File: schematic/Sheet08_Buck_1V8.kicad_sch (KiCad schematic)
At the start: 15 parts, among them U6 ISL70003ASEH

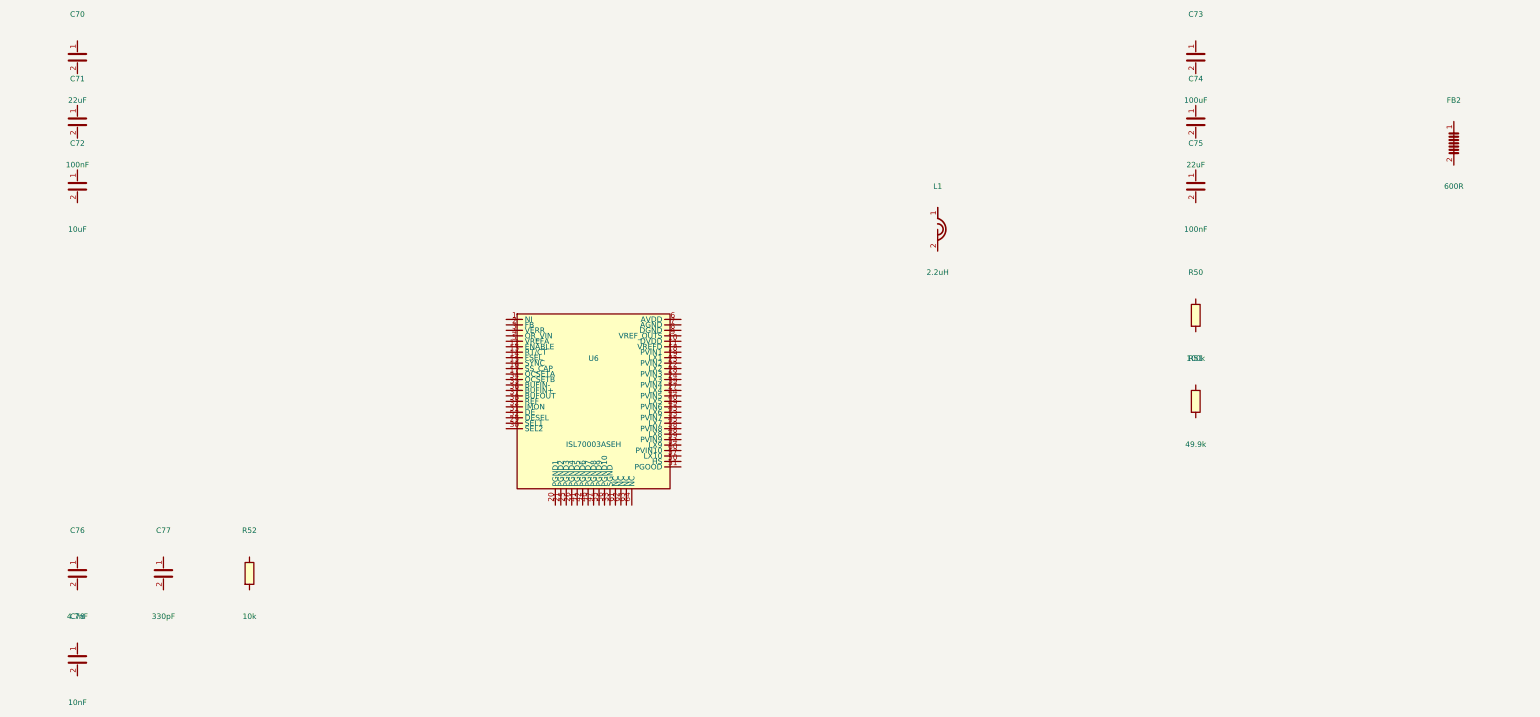
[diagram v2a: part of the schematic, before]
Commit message: feat: add 745 wire connections linking all IC pins to labels and power symbols
- Added stub wires from every component pin to net labels/global_labels
- Power pins connected to correct power symbols (GND, +1V0, +1V8, +3V3, etc.)
- Signal pins connected to labeled nets matching design spec
- Global labels for cross-sheet signals (JESD, SPI, clock, SpaceWire)
- Fixed missing +3V3 power symbol definitions in 5 sheets
- All 17 sheets export successfully with KiCad CLI (17/17 OK)
- Merged PDF: 3.1MB, 17 pages with visible wire connections
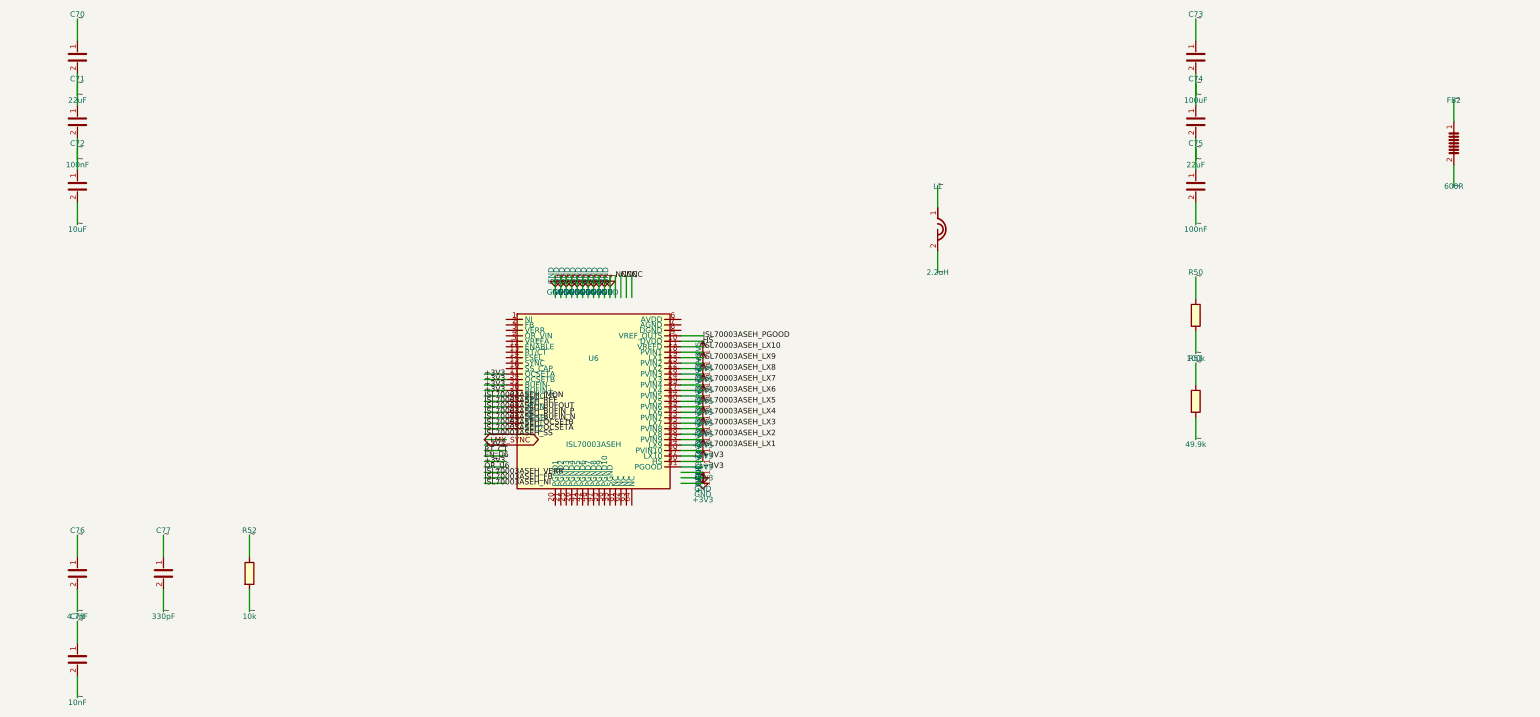
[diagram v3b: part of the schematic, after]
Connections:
- net ~: now reaches C73.1
- net ~: now also C70.1, C70.2, C71.1, C71.2, C72.1, C72.2, C73.2, C74.1, C74.2, C75.1, C75.2, C76.1, C76.2, C77.1, C77.2, C78.1, C78.2, FB2.1, FB2.2, L1.1, L1.2, R50.1, R50.2, R51.1, R51.2, R52.1, R52.2
- net HS: now reaches U6.10 (DVDD)
- net ISL70003ASEH_LX10: now reaches U6.11 (VREFD)
- net +3V3: now reaches U6.17 (OCSETA)
- net +3V3: now also U6.34 (OCSETB), U6.35 (BUFIN-), U6.36 (BUFIN+), U6.50 (HS), U6.51 (PGOOD), U6.57 (LX10)
- net +4V5: now reaches U6.18 (PVIN1)
- net +4V5: now also U6.23 (PVIN2), U6.28 (PVIN3), U6.39 (PVIN4), U6.44 (PVIN5), U6.49 (PVIN6), U6.53 (PVIN7), U6.58 (PVIN8), U6.59 (PVIN9), U6.60 (PVIN10)
- net ISL70003ASEH_LX9: now reaches U6.19 (LX1)
- net ISL70003ASEH_LX8: now reaches U6.22 (LX2)
- net ISL70003ASEH_LX7: now reaches U6.24 (LX3)
- net ISL70003ASEH_LX6: now reaches U6.27 (LX4)
- net ISL70003ASEH_OCSETB: now reaches U6.29 (SEL1)
- net ISL70003ASEH_OCSETA: now reaches U6.30 (SEL2)
- net ISL70003ASEH_BUFIN_P: now reaches U6.31 (DE)
- net ISL70003ASEH_BUFOUT: now reaches U6.32 (IMON)
- net ISL70003ASEH_IMON: now reaches U6.37 (BUFOUT)
- net ISL70003ASEH_REF: now reaches U6.38 (REF)
- net ISL70003ASEH_LX5: now reaches U6.40 (LX5)
- net ISL70003ASEH_LX4: now reaches U6.43 (LX6)
- net ISL70003ASEH_LX3: now reaches U6.45 (LX7)
- net ISL70003ASEH_LX2: now reaches U6.48 (LX8)
- net ISL70003ASEH_BUFIN_N: now reaches U6.52 (DESEL)
- net ISL70003ASEH_LX1: now reaches U6.54 (LX9)
- net ISL70003ASEH_PGOOD: now reaches U6.9 (VREF_OUTS)

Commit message: Fix KiCad schematic wiring: Y-inversion bug + all 891 pins connected
- Fixed critical Y-axis inversion bug: KiCad inverts Y when placing
  symbols (lib Y + schematic Y = abs Y is WRONG; correct: abs Y = sym Y - lib Y)
- This caused ALL wires to connect to wrong pins (e.g., CS label connected
  to BG pin instead of CS pin)
- Verified with netlist: 0 unconnected nets, all pin functions correct
- Fixed wire direction for angle 90/270 (swapped due to Y-inversion)
- 891 pin connections across 15 sheets, all 17 sheets export without errors
- Netlist verification: CS→E8, BG→C3, INA+→A4, CLK+→F1, JESD pairs correct

Co-Authored-By: opencode <noreply@opencode.ai>
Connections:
- net +3V3: now also U6.10 (DVDD), U6.11 (VREFD), U6.14 (FSEL), U6.29 (SEL1), U6.30 (SEL2), U6.31 (DE), U6.5 (VREFA), U6.52 (DESEL), U6.6 (AVDD), U6.9 (VREF_OUTS); no longer U6.17 (OCSETA), U6.34 (OCSETB), U6.35 (BUFIN-), U6.36 (BUFIN+), U6.50 (HS), U6.51 (PGOOD), U6.57 (LX10)
- net EN_U6: now also U6.12 (ENABLE)
- net GND: now also U6.20 (PGND1), U6.21 (PGND2), U6.25 (PGND3), U6.26 (PGND4), U6.33 (SGND), U6.41 (PGND5), U6.42 (PGND6), U6.46 (PGND7), U6.47 (PGND8), U6.55 (PGND9), U6.56 (PGND10), U6.7 (AGND), U6.8 (DGND)
- net HS: now also U6.50 (HS); no longer U6.10 (DVDD)
- net ISL70003ASEH_BUFIN_N: now also U6.35 (BUFIN-); no longer U6.52 (DESEL)
- net ISL70003ASEH_BUFIN_P: now also U6.36 (BUFIN+); no longer U6.31 (DE)
- net ISL70003ASEH_BUFOUT: now also U6.37 (BUFOUT); no longer U6.32 (IMON)
- net ISL70003ASEH_FB: now also U6.2 (FB)
- net ISL70003ASEH_IMON: now also U6.32 (IMON); no longer U6.37 (BUFOUT)
- net ISL70003ASEH_LX1: now also U6.19 (LX1); no longer U6.54 (LX9)
- net ISL70003ASEH_LX10: now also U6.57 (LX10); no longer U6.11 (VREFD)
- net ISL70003ASEH_LX2: now also U6.22 (LX2); no longer U6.48 (LX8)
- net ISL70003ASEH_LX3: now also U6.24 (LX3); no longer U6.45 (LX7)
- net ISL70003ASEH_LX4: now also U6.27 (LX4); no longer U6.43 (LX6)
- net ISL70003ASEH_LX6: now also U6.43 (LX6); no longer U6.27 (LX4)
- net ISL70003ASEH_LX7: now also U6.45 (LX7); no longer U6.24 (LX3)
- net ISL70003ASEH_LX8: now also U6.48 (LX8); no longer U6.22 (LX2)
- net ISL70003ASEH_LX9: now also U6.54 (LX9); no longer U6.19 (LX1)
- net ISL70003ASEH_NI: now also U6.1 (NI)
- net ISL70003ASEH_OCSETA: now also U6.17 (OCSETA); no longer U6.30 (SEL2)
- net ISL70003ASEH_OCSETB: now also U6.34 (OCSETB); no longer U6.29 (SEL1)
- net ISL70003ASEH_PGOOD: now also U6.51 (PGOOD); no longer U6.9 (VREF_OUTS)
- net ISL70003ASEH_SS: now also U6.16 (SS_CAP)
- net ISL70003ASEH_VERR: now also U6.3 (VERR)
- net LMX_SYNC: now also U6.15 (SYNC)
- net NC: now also U6.61 (NC), U6.62 (NC), U6.63 (NC), U6.64 (NC)
- net OR_U6: now also U6.4 (OR_VIN)
- net RT_CT: now also U6.13 (RT/CT)
- net +4V5 renamed VIN

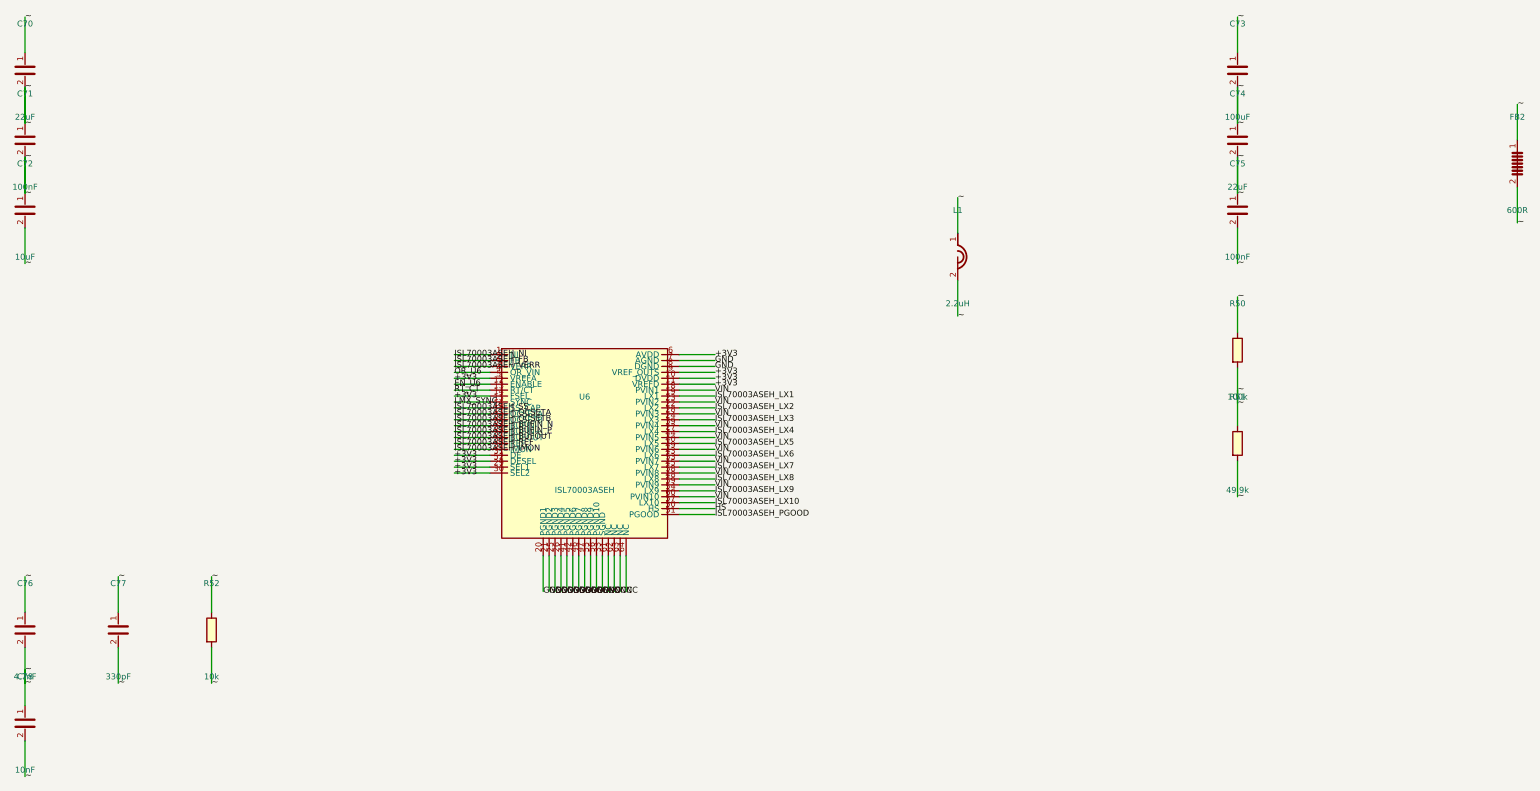
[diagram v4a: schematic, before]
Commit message: fix: use horizontal wire stubs to prevent KiCad net merging
Root cause: vertical wires from stacked power pins (1.27mm spacing)
overlapped when wire length > pin spacing, causing KiCad to merge
all power nets into one. Also skip unnamed (~) passive component pins.

Changes:
- Always use horizontal LEFT stubs regardless of pin angle
- Skip pins with net_name '~' (capacitor/resistor unnamed pins)
- 557 pin connections across 13 sheets, all pass KiCad CLI

NOTE: power net separation still shows all power_in pins on one net
in kicad-cli netlist export - needs further investigation.
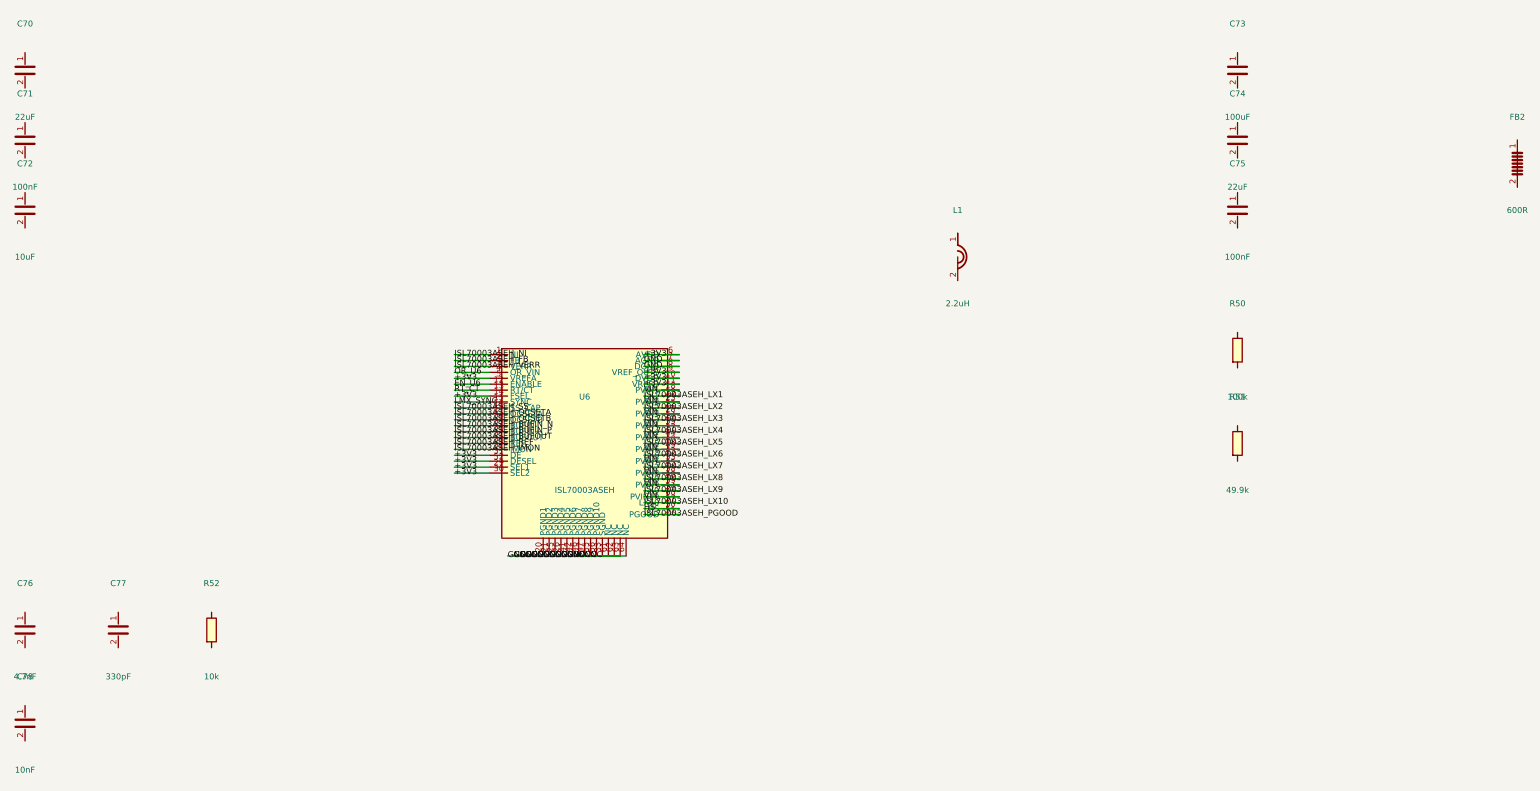
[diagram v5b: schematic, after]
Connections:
- net NC is gone; now on net GND: U6.61 (NC), U6.62 (NC), U6.63 (NC), U6.64 (NC)
- removed net ~: C70.1, C70.2, C71.1, C71.2, C72.1, C72.2, C73.1, C73.2, C74.1, C74.2, C75.1, C75.2, C76.1, C76.2, C77.1, C77.2, C78.1, C78.2, FB2.1, FB2.2, L1.1, L1.2, R50.1, R50.2, R51.1, R51.2, R52.1, R52.2

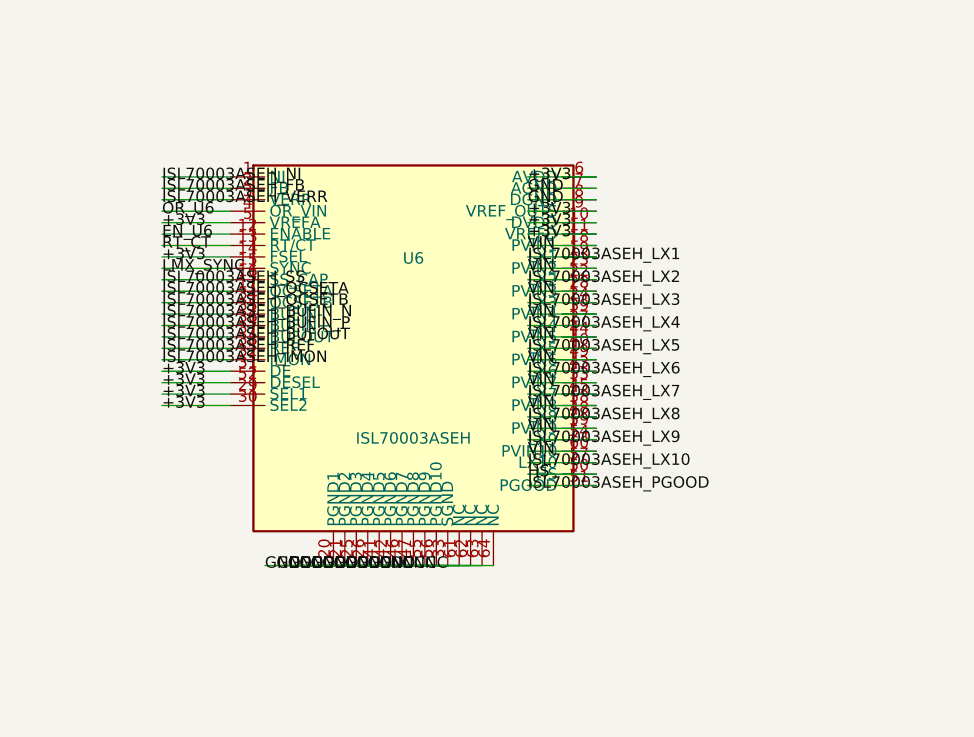
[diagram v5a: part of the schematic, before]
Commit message: fix: replace wire stubs with labels-only to prevent power net shorts
Labels placed directly at pin endpoints eliminate wire overlap that
caused BGA power pins (VA11, VA19, VD11, AGND, DGND) to merge into
a single net. Verified via netlist: GND=52, +1V0_ANA=12, +1V9_ANA=12,
+1V1_DIG=10 nodes (all correct per datasheet pin mapping).
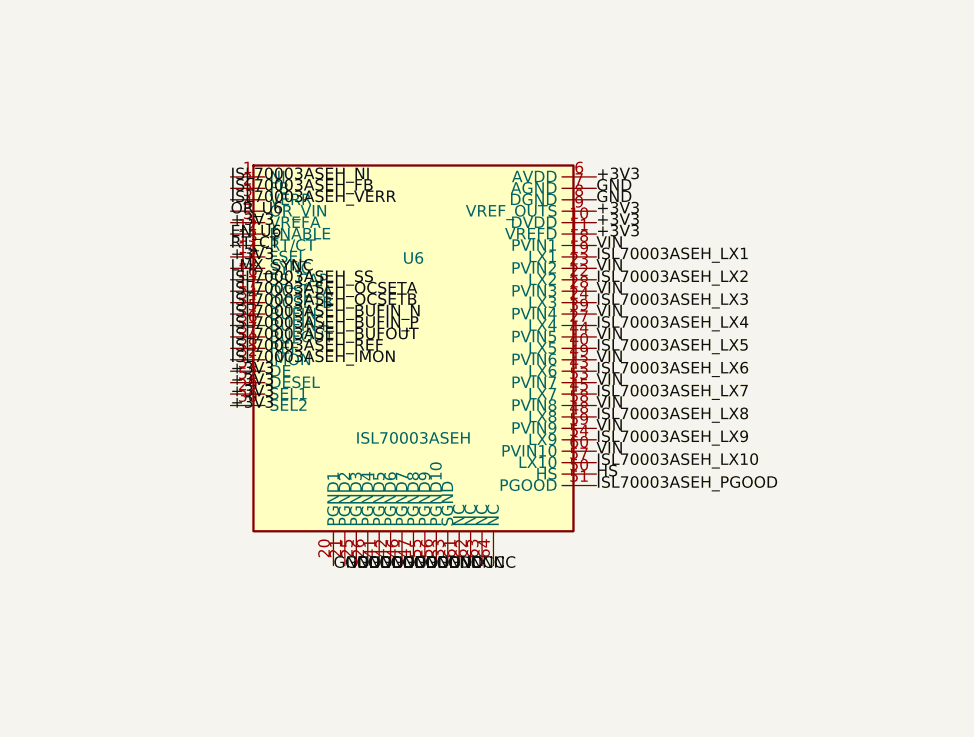
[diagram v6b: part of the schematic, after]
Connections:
- net GND: no longer U6.61 (NC), U6.62 (NC), U6.63 (NC), U6.64 (NC)
- new net NC: U6.61 (NC), U6.62 (NC), U6.63 (NC), U6.64 (NC)

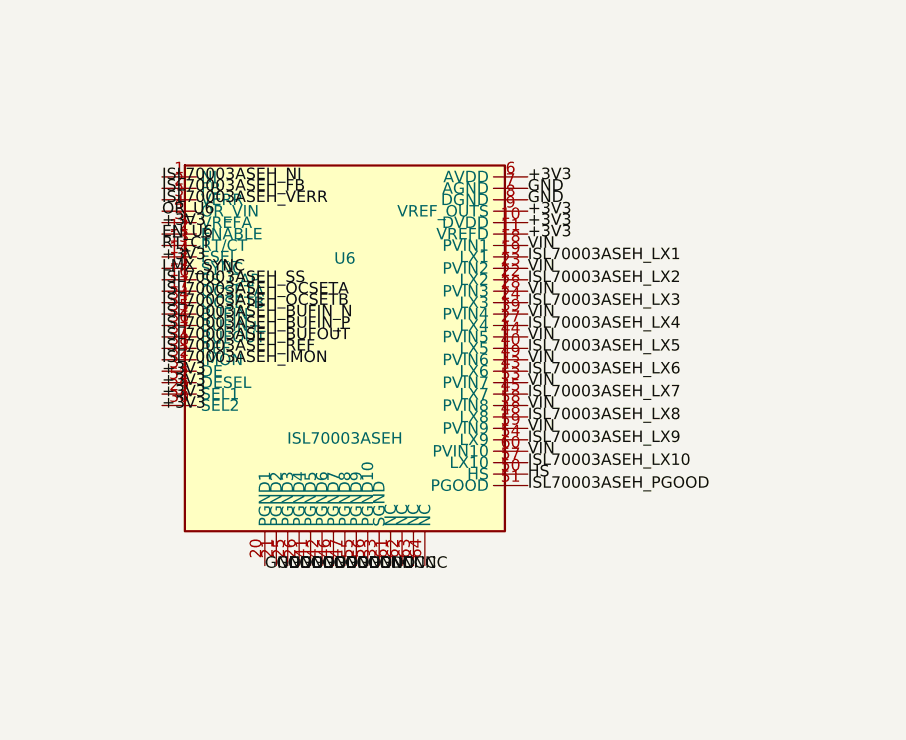
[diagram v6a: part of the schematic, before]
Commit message: fix: isolate ISL70003ASEH buck pins, fix LMX_SYNC collision, NC pins, connector pin names
- ISL70003ASEH pins now use ref prefix (U6_LX1 vs U7_LX1) to prevent shorts
- Buck SYNC pins separated from LMX_SYNC (power sync ≠ PLL sync)
- NC pins properly skipped (unconnected)
- Connector PIN_1..PIN_6 use ref prefix (J1_PIN_1 vs J2_PIN_1)
- Fixed annotation warnings in Sheet13 (C_dev→C125, R_dev→R74, U_TPS7H→U14)
- Regenerated all PDFs and SVGs
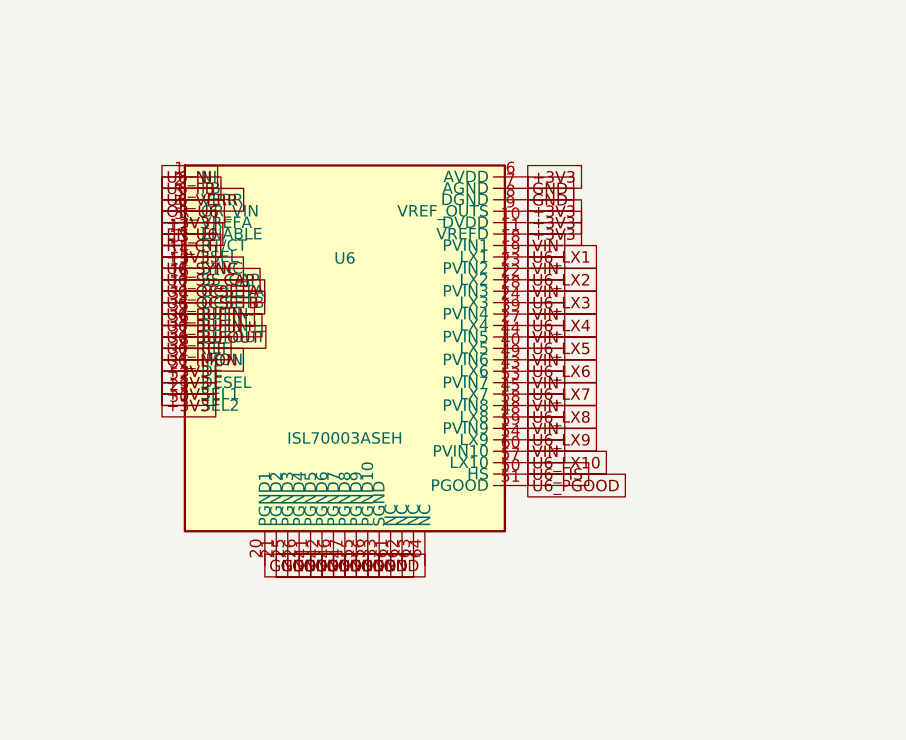
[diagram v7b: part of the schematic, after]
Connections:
- net HS renamed U6_HS
- net ISL70003ASEH_BUFIN_N renamed U6_BUFIN-
- net ISL70003ASEH_BUFIN_P renamed U6_BUFIN+
- net ISL70003ASEH_BUFOUT renamed U6_BUFOUT
- net ISL70003ASEH_FB renamed U6_FB
- net ISL70003ASEH_IMON renamed U6_IMON
- net ISL70003ASEH_LX1 renamed U6_LX1
- net ISL70003ASEH_LX10 renamed U6_LX10
- net ISL70003ASEH_LX2 renamed U6_LX2
- net ISL70003ASEH_LX3 renamed U6_LX3
- net ISL70003ASEH_LX4 renamed U6_LX4
- net ISL70003ASEH_LX5 renamed U6_LX5
- net ISL70003ASEH_LX6 renamed U6_LX6
- net ISL70003ASEH_LX7 renamed U6_LX7
- net ISL70003ASEH_LX8 renamed U6_LX8
- net ISL70003ASEH_LX9 renamed U6_LX9
- net ISL70003ASEH_NI renamed U6_NI
- net ISL70003ASEH_OCSETA renamed U6_OCSETA
- net ISL70003ASEH_OCSETB renamed U6_OCSETB
- net ISL70003ASEH_PGOOD renamed U6_PGOOD
- net ISL70003ASEH_REF renamed U6_REF
- net ISL70003ASEH_SS renamed U6_SS_CAP
- net ISL70003ASEH_VERR renamed U6_VERR
- net LMX_SYNC renamed U6_SYNC
- removed net NC: U6.61 (NC), U6.62 (NC), U6.63 (NC), U6.64 (NC)
